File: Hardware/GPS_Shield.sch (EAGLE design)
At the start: 52 parts, among them J1 ARDUINO_R3_SHIELD, J2 USD_CONNECTOR, J3 DNP (GP-735-VERTICAL), U1 APK2112-3.3V, U2 GP3906-TLP, U3 TXB0108

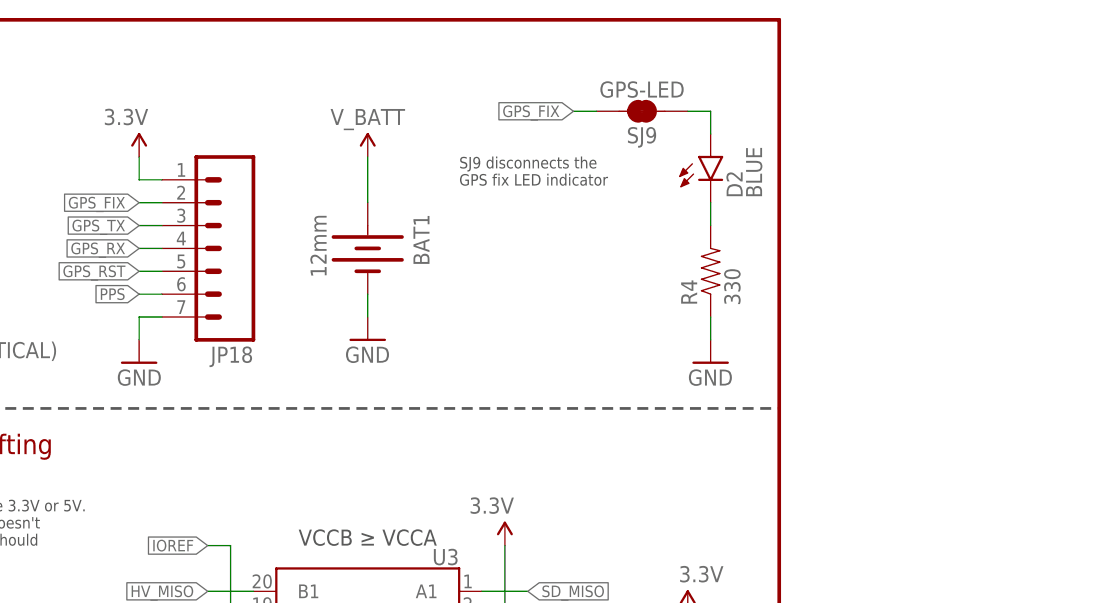
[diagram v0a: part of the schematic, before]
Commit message: Adding VBATT-to-3.3V jumper, breaking out VBATT.
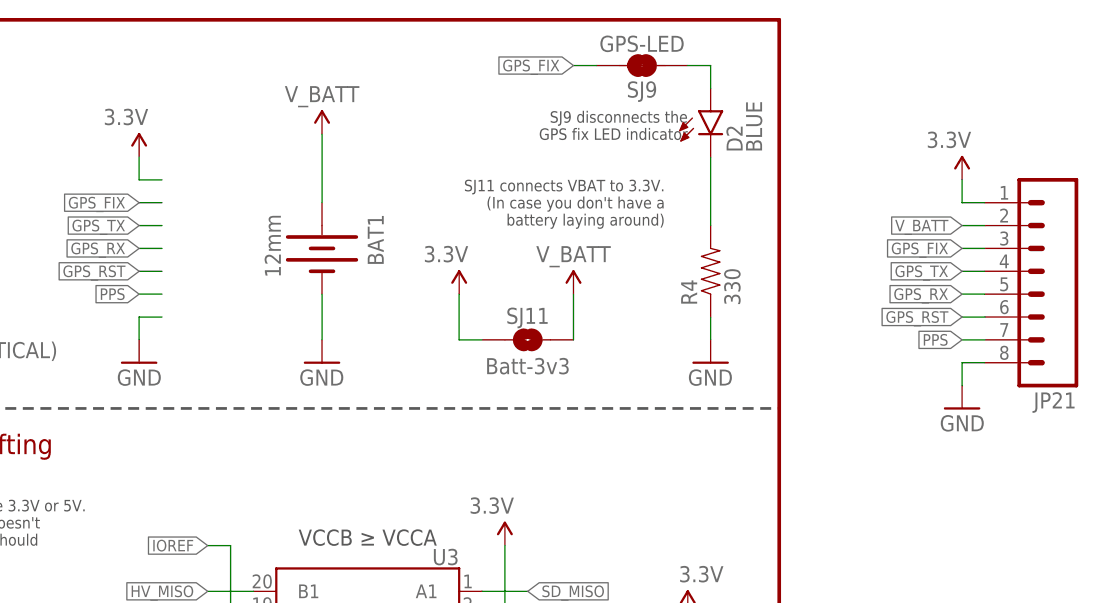
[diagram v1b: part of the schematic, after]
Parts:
- removed JP18: (no value), SparkFun-Connectors:M07NO_SILK
- added JP21: (no value), SparkFun-Connectors:M08NO_SILK_FEMALE_PTH
- added SJ11: Batt-3v3, SparkFun-Passives:JUMPER-PAD-2-NOYES_SILK
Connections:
- net 3.3V: now also JP21.1, SJ11.1; no longer JP18.1
- net GND: now also JP21.8; no longer JP18.7
- net GPS_FIX: now also JP21.3; no longer JP18.2
- net GPS_RST: now also JP21.6; no longer JP18.5
- net GPS_RX: now also JP21.5; no longer JP18.4
- net GPS_TX: now also JP21.4; no longer JP18.3
- net PPS: now also JP21.7; no longer JP18.6
- net V_BATT: now also JP21.2, SJ11.2
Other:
- note added: "SJ11 connects VBAT to 3.3V. (In case you don't have a battery laying around)"
- moved on the sheet: BAT1, D2, SJ9

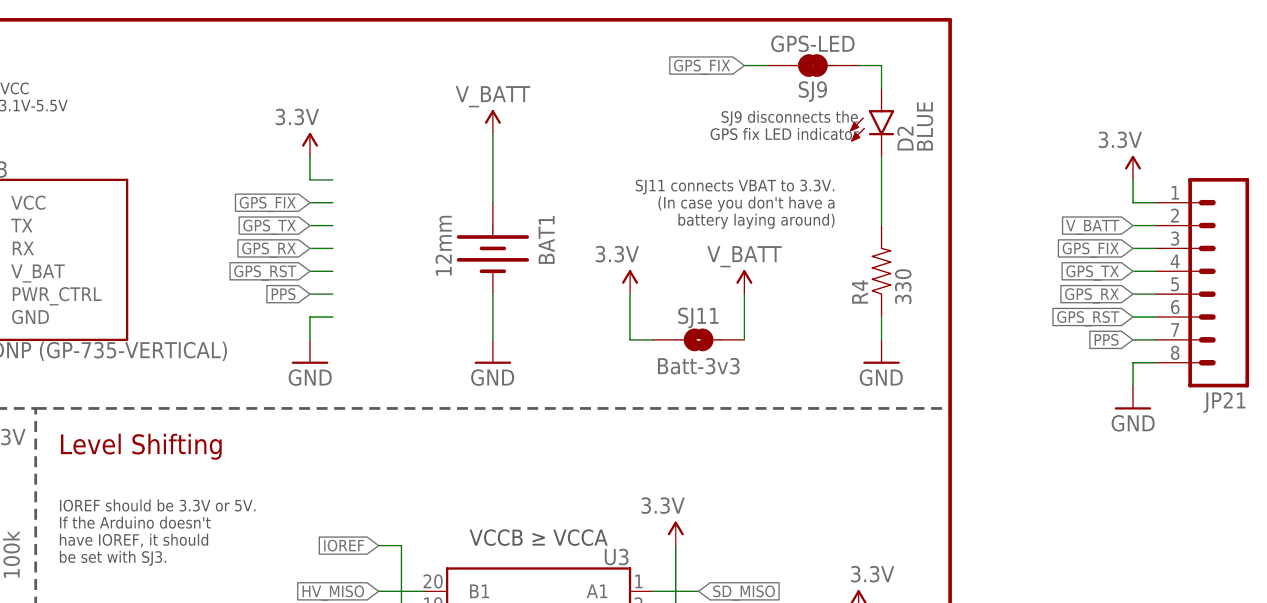
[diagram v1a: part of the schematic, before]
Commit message: Schematic and trace cleanup.
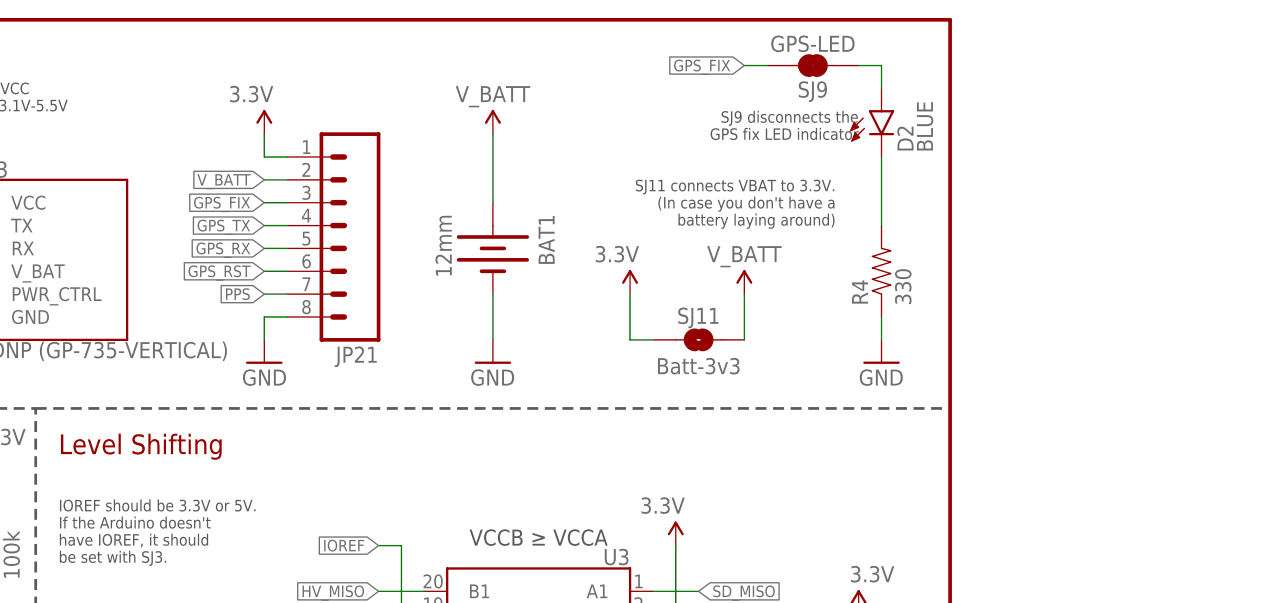
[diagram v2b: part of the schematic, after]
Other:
- moved on the sheet: JP21
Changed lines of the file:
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@@
 <part name="JP6" library="SparkFun-Connectors" deviceset="M10" device="NO_SILK_PTH_FEMALE"/>
 <part name="JP3" library="SparkFun-Connectors" deviceset="M07" device="NO_SILK"/>
-<part name="P+8" library="SparkFun" deviceset="3.3V" device=""/>
-<part name="GND14" library="SparkFun" deviceset="GND" device=""/>
 <part name="LOGO2" library="SparkFun-Aesthetics" deviceset="SFE_LOGO_NAME_FLAME" device=".1_INCH" value="SFE_LOGO_NAME_FLAME.1_INCH"/>
 <part name="LOGO1" library="SparkFun-Aesthetics" deviceset="OSHW-LOGO" device="M" value="OSHW-LOGOM"/>
@@
 <attribute name="NAME" x="1.778" y="119.38" size="1.778" layer="95" rot="R90"/>
 </instance>
-<instance part="P+8" gate="G$1" x="177.8" y="170.18" rot="MR0"/>
-<instance part="GND14" gate="1" x="177.8" y="147.32" rot="MR0"/>
 <instance part="LOGO2" gate="G$1" x="190.5" y="35.56"/>
 <instance part="LOGO1" gate="G$1" x="109.22" y="10.16"/>
@@
 <attribute name="VALUE" x="226.06" y="158.496" size="1.778" layer="96" align="bottom-center"/>
 </instance>
-<instance part="JP21" gate="G$1" x="276.86" y="157.48" rot="R180"/>
-<instance part="P+13" gate="G$1" x="269.24" y="167.64" rot="MR0"/>
-<instance part="GND19" gate="1" x="269.24" y="142.24" rot="MR0"/>
+<instance part="JP21" gate="G$1" x="180.34" y="162.56" rot="R180"/>
+<instance part="P+13" gate="G$1" x="172.72" y="172.72" rot="MR0"/>
+<instance part="GND19" gate="1" x="172.72" y="147.32" rot="MR0"/>
 </instances>
 <busses>
@@
 <pinref part="GND5" gate="1" pin="GND"/>
 <wire x1="30.48" y1="78.74" x2="30.48" y2="76.2" width="0.1524" layer="91"/>
-</segment>
-<segment>
-<pinref part="GND14" gate="1" pin="GND"/>
-<wire x1="180.34" y1="152.4" x2="177.8" y2="152.4" width="0.1524" layer="91"/>
-<wire x1="177.8" y1="152.4" x2="177.8" y2="149.86" width="0.1524" layer="91"/>
 </segment>
 <segment>
@@
 <segment>
 <pinref part="JP21" gate="G$1" pin="8"/>
-<wire x1="271.78" y1="147.32" x2="269.24" y2="147.32" width="0.1524" layer="91"/>
-<wire x1="269.24" y1="147.32" x2="269.24" y2="144.78" width="0.1524" layer="91"/>
+<wire x1="175.26" y1="152.4" x2="172.72" y2="152.4" width="0.1524" layer="91"/>
+<wire x1="172.72" y1="152.4" x2="172.72" y2="149.86" width="0.1524" layer="91"/>
 <pinref part="GND19" gate="1" pin="GND"/>
 </segment>
@@
 </segment>
 <segment>
-<wire x1="180.34" y1="167.64" x2="177.8" y2="167.64" width="0.1524" layer="91"/>
-<wire x1="177.8" y1="167.64" x2="177.8" y2="170.18" width="0.1524" layer="91"/>
-<pinref part="P+8" gate="G$1" pin="3.3V"/>
-</segment>
-<segment>
 <pinref part="SJ1" gate="G$1" pin="1"/>
 <wire x1="20.32" y1="45.72" x2="17.78" y2="45.72" width="0.1524" layer="91"/>
@@
 <segment>
 <pinref part="JP21" gate="G$1" pin="1"/>
-<wire x1="271.78" y1="165.1" x2="269.24" y2="165.1" width="0.1524" layer="91"/>
-<wire x1="269.24" y1="165.1" x2="269.24" y2="167.64" width="0.1524" layer="91"/>
+<wire x1="175.26" y1="170.18" x2="172.72" y2="170.18" width="0.1524" layer="91"/>
+<wire x1="172.72" y1="170.18" x2="172.72" y2="172.72" width="0.1524" layer="91"/>
 <pinref part="P+13" gate="G$1" pin="3.3V"/>
 </segment>
@@
 </segment>
 <segment>
-<wire x1="180.34" y1="154.94" x2="177.8" y2="154.94" width="0.1524" layer="91"/>
-<label x="177.8" y="154.94" size="1.27" layer="95" rot="MR0" xref="yes"/>
-</segment>
-<segment>
 <pinref part="JP21" gate="G$1" pin="7"/>
-<wire x1="271.78" y1="149.86" x2="269.24" y2="149.86" width="0.1524" layer="91"/>
-<label x="269.24" y="149.86" size="1.27" layer="95" rot="R180" xref="yes"/>
+<wire x1="175.26" y1="154.94" x2="172.72" y2="154.94" width="0.1524" layer="91"/>
+<label x="172.72" y="154.94" size="1.27" layer="95" rot="R180" xref="yes"/>
 </segment>
 </net>
@@
 <segment>
 <pinref part="JP21" gate="G$1" pin="2"/>
-<wire x1="271.78" y1="162.56" x2="269.24" y2="162.56" width="0.1524" layer="91"/>
-<label x="269.24" y="162.56" size="1.27" layer="95" rot="R180" xref="yes"/>
+<wire x1="175.26" y1="167.64" x2="172.72" y2="167.64" width="0.1524" layer="91"/>
+<label x="172.72" y="167.64" size="1.27" layer="95" rot="R180" xref="yes"/>
 </segment>
 </net>
@@
 </segment>
 <segment>
-<wire x1="180.34" y1="160.02" x2="177.8" y2="160.02" width="0.1524" layer="91"/>
-<label x="177.8" y="160.02" size="1.27" layer="95" rot="MR0" xref="yes"/>
-</segment>
-<segment>
 <pinref part="JP21" gate="G$1" pin="5"/>
-<wire x1="271.78" y1="154.94" x2="269.24" y2="154.94" width="0.1524" layer="91"/>
-<label x="269.24" y="154.94" size="1.27" layer="95" rot="R180" xref="yes"/>
+<wire x1="175.26" y1="160.02" x2="172.72" y2="160.02" width="0.1524" layer="91"/>
+<label x="172.72" y="160.02" size="1.27" layer="95" rot="R180" xref="yes"/>
 </segment>
 </net>
@@
 </segment>
 <segment>
-<wire x1="180.34" y1="162.56" x2="177.8" y2="162.56" width="0.1524" layer="91"/>
-<label x="177.8" y="162.56" size="1.27" layer="95" rot="MR0" xref="yes"/>
-</segment>
-<segment>
 <pinref part="JP21" gate="G$1" pin="4"/>
-<wire x1="271.78" y1="157.48" x2="269.24" y2="157.48" width="0.1524" layer="91"/>
-<label x="269.24" y="157.48" size="1.27" layer="95" rot="R180" xref="yes"/>
+<wire x1="175.26" y1="162.56" x2="172.72" y2="162.56" width="0.1524" layer="91"/>
+<label x="172.72" y="162.56" size="1.27" layer="95" rot="R180" xref="yes"/>
 </segment>
 </net>
@@
 </segment>
 <segment>
-<wire x1="180.34" y1="165.1" x2="177.8" y2="165.1" width="0.1524" layer="91"/>
-<label x="177.8" y="165.1" size="1.27" layer="95" rot="MR0" xref="yes"/>
-</segment>
-<segment>
 <pinref part="SJ9" gate="G$1" pin="2"/>
 <wire x1="228.6" y1="180.34" x2="226.06" y2="180.34" width="0.1524" layer="91"/>
@@
 <segment>
 <pinref part="JP21" gate="G$1" pin="3"/>
-<wire x1="271.78" y1="160.02" x2="269.24" y2="160.02" width="0.1524" layer="91"/>
-<label x="269.24" y="160.02" size="1.27" layer="95" rot="R180" xref="yes"/>
+<wire x1="175.26" y1="165.1" x2="172.72" y2="165.1" width="0.1524" layer="91"/>
+<label x="172.72" y="165.1" size="1.27" layer="95" rot="R180" xref="yes"/>
 </segment>
 </net>
@@
 </segment>
 <segment>
-<wire x1="180.34" y1="157.48" x2="177.8" y2="157.48" width="0.1524" layer="91"/>
-<label x="177.8" y="157.48" size="1.27" layer="95" rot="MR0" xref="yes"/>
-</segment>
-<segment>
 <pinref part="JP21" gate="G$1" pin="6"/>
-<wire x1="271.78" y1="152.4" x2="269.24" y2="152.4" width="0.1524" layer="91"/>
-<label x="269.24" y="152.4" size="1.27" layer="95" rot="R180" xref="yes"/>
-</segment>
-</net>
+<wire x1="175.26" y1="157.48" x2="172.72" y2="157.48" width="0.1524" layer="91"/>
+<label x="172.72" y="157.48" size="1.27" layer="95" rot="R180" xref="yes"/>
+</segment>
+</net>

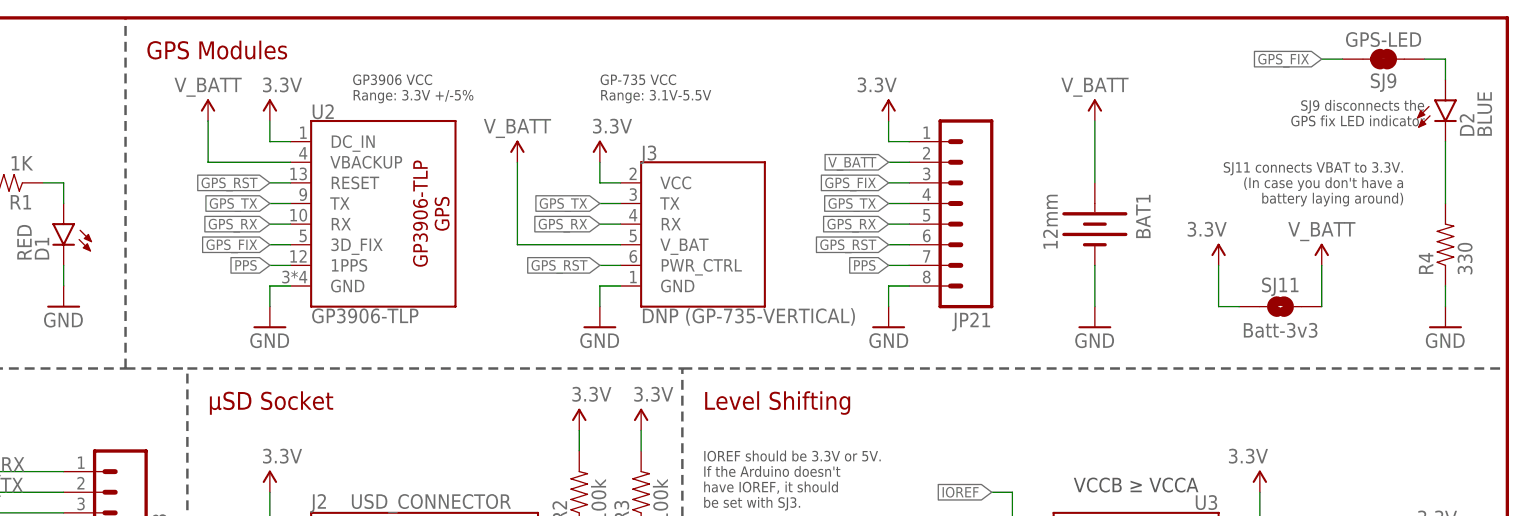
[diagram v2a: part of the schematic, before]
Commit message: Removing GP-735 fp. Default 3.3/VBat jumper closed.
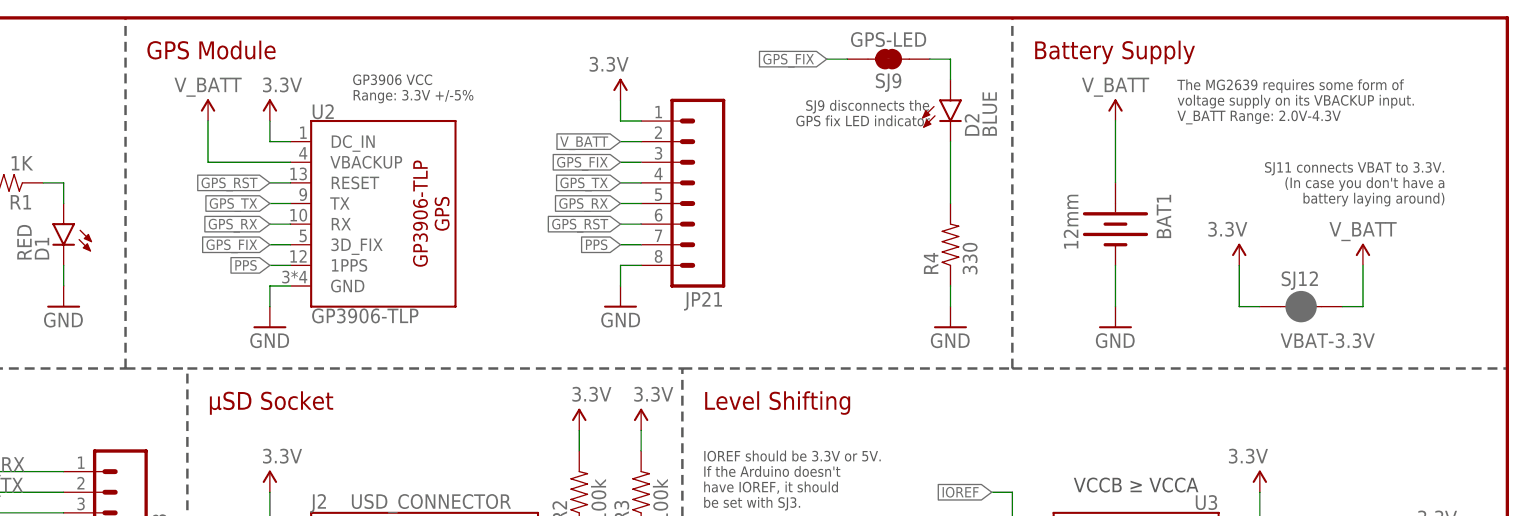
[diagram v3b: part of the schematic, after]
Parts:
- removed J3: DNP (GP-735-VERTICAL), SparkFun-RF:GP-735-VERTICAL
- removed SJ11: Batt-3v3, SparkFun-Passives:JUMPER-PAD-2-NOYES_SILK
- added SJ12: VBAT-3.3V, SparkFun-Passives:JUMPER-PAD-2-NC_BY_PASTE
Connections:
- net 3.3V: now also SJ12.1; no longer J3.VCC, SJ11.1
- net GND: no longer J3.GND
- net GPS_RST: no longer J3.PWR_CTRL
- net GPS_RX: no longer J3.RX
- net GPS_TX: no longer J3.TX
- net V_BATT: now also SJ12.2; no longer J3.V_BAT, SJ11.2
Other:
- note added: "Battery Supply"
- note added: "GPS Module"
- note added: "The MG2639 requires some form of voltage supply on its VBACKUP input. V_BATT Range: 2.0V-4.3V"
- note removed: "GP-735 VCC Range: 3.1V-5.5V"
- note removed: "GPS Modules"
- moved on the sheet: BAT1, D2, JP21, R4, SJ9
